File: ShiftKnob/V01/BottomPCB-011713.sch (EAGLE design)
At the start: 37 parts, among them IC2 7805DT, Q1 16MHz, Q2 MOSFET-NCHANNELSMD, Q3 MOSFET-PCHANNELSMD, Q4 MOSFET-NCHANNELSMD, Q5 MOSFET-NCHANNELSMD, Q6 MOSFET-NCHANNELSMD, U1 ATMEGA328

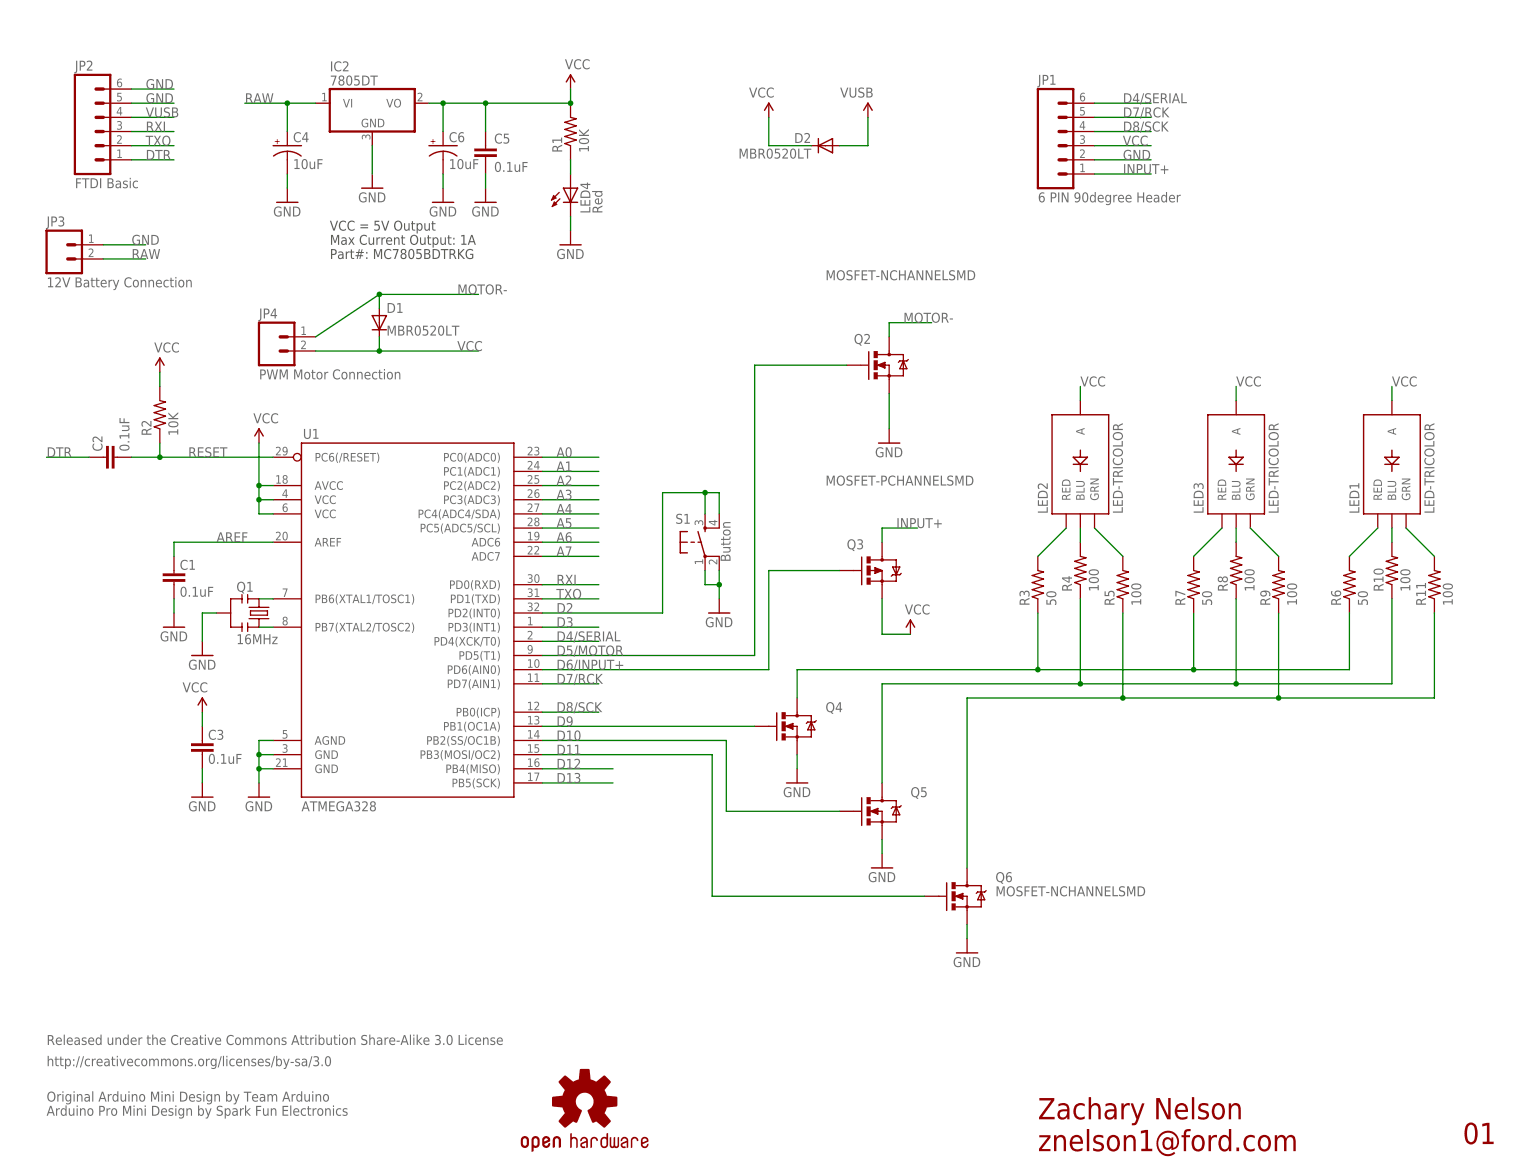
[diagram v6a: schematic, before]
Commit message: update with new frames and printed drawings for assembly.
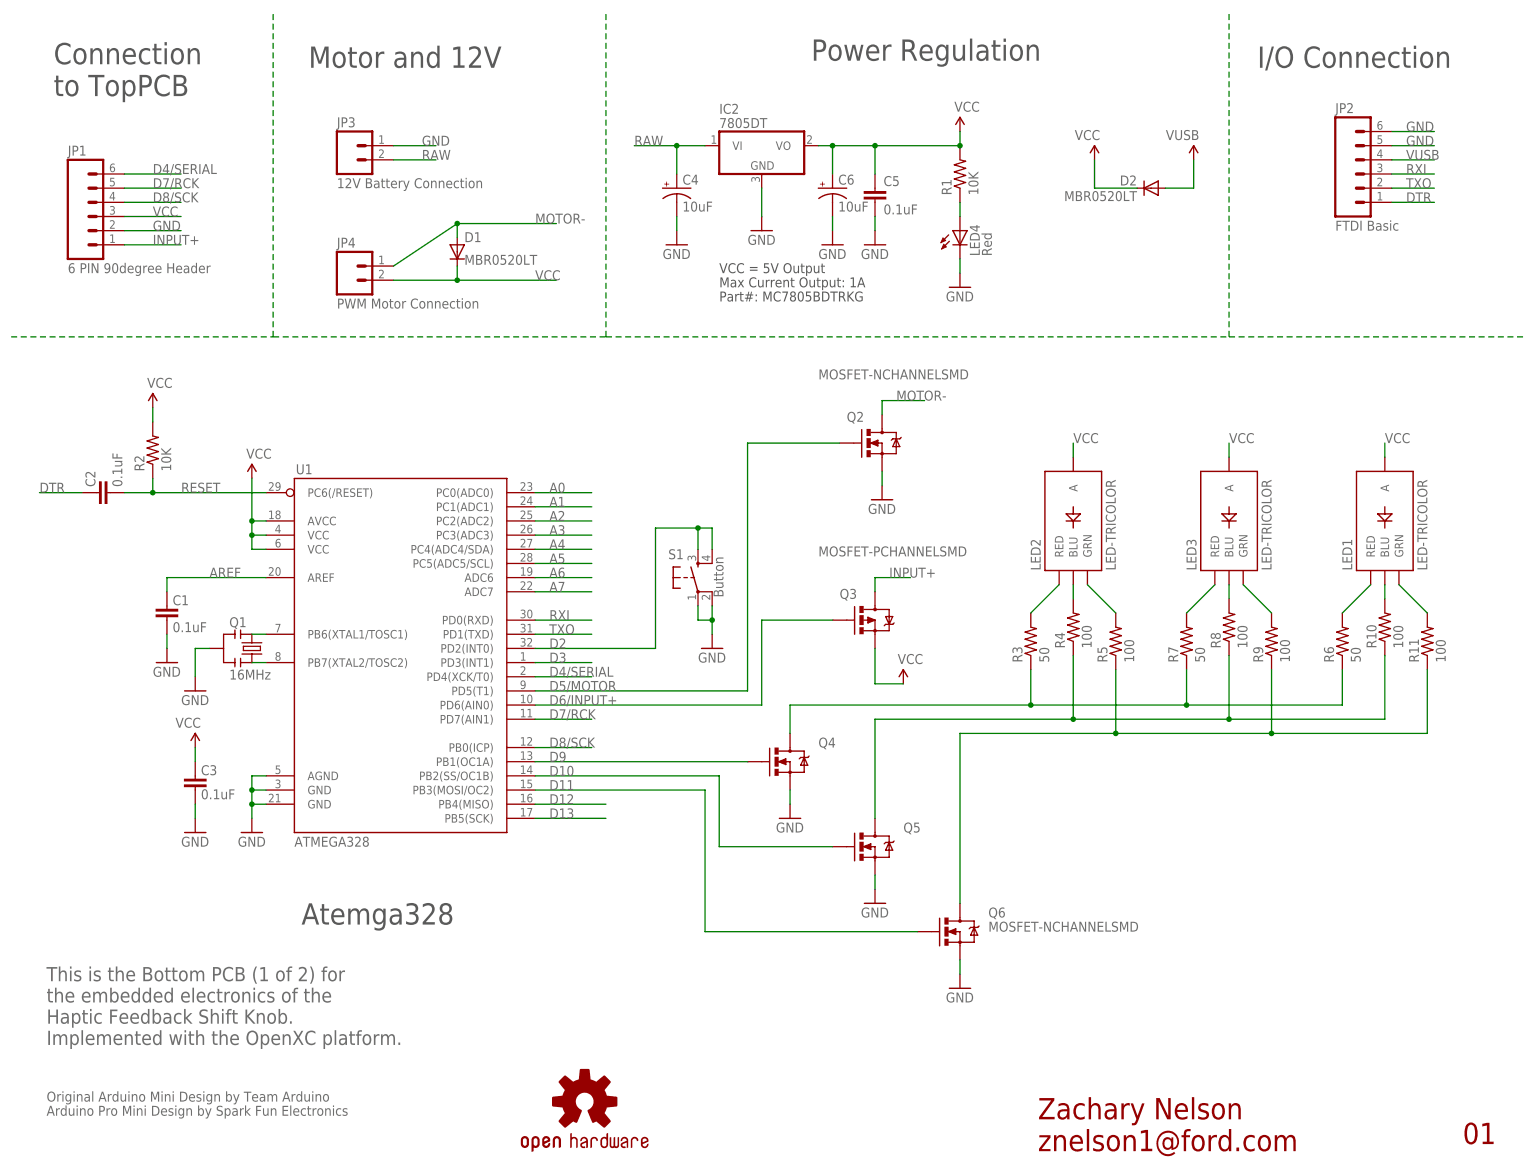
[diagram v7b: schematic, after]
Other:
- note added: "Atemga328"
- note added: "Connection to TopPCB"
- note added: "I/O Connection"
- note added: "Motor and 12V"
- note added: "Power Regulation"
- note added: "This is the Bottom PCB (1 of 2) for the embedded electronics of the Haptic Feedback Shift Knob. Implemented with the OpenXC platform."
- note removed: "Released under the Creative Commons Attribution Share-Alike 3.0 License"
- note removed: "http://creativecommons.org/licenses/by-sa/3.0"
- moved on the sheet: C1, C2, C3, C4, C5, C6, D1, D2, IC2, JP1, JP2, JP3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
